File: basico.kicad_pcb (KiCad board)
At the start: 2 copper layers, 85.9 x 99.9 mm, 8 parts, among them P1 Power, P2 Analog, P3 Analog, P4 Digital, P5 PWM, P6 PWM, P7 Communication

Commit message: All routes done
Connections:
- P4 pad 1: GND -> (no net)
- P4 pad 2: GND -> (no net)
- P4 pad 35: +5V -> (no net)
- P4 pad 36: +5V -> (no net)
- XA101 pad 1: +3.3VP -> (no net)
- XA101 pad 2: +5V -> (no net)
- XA101 pad 20: GND -> (no net)
- XA101 pad 22: GND -> (no net)
- XA101 pad 24: GND -> (no net)
- XA101 pad 26: GND -> (no net)
- XA101 pad 28: GND -> (no net)
- XA101 pad 30: GND -> (no net)
- XA101 pad 32: GND -> (no net)
- XA101 pad 38: GND -> (no net)
- XA101 pad 4: GND -> (no net)
- XA101 pad 40: GND -> (no net)
- XA101 pad 51: GND -> (no net)
- XA101 pad 53: GND -> (no net)
- XA101 pad 57: GND -> (no net)
- XA101 pad 59: GND -> (no net)
- XA101 pad 65: GND -> (no net)
- XA101 pad 67: GND -> (no net)
- XA101 pad 77: GND -> (no net)
- XA101 pad 79: GND -> (no net)
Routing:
- net /Ar_38: track 0.00 -> 154.9 mm, vias 0 -> 2
- net /Ar_34: track 0.00 -> 120.1 mm, vias 0 -> 1
- net /Ar_17: track 0.00 -> 109.1 mm, vias 0 -> 1
- net /Ar_42: track 0.00 -> 88.5 mm, vias 0 -> 1
- net /Ar_A4: track 0.00 -> 77.7 mm, vias 0 -> 1
- net /Ar_11: track 0.00 -> 75.5 mm
- net /Ar_36: track 0.00 -> 73.3 mm
- net /Ar_16: track 0.00 -> 69.6 mm
- net /Ar_4: track 0.00 -> 69.3 mm
- net /Ar_A11: track 0.00 -> 67.9 mm, vias 0 -> 1
- net /Ar_A10: track 0.00 -> 66.2 mm, vias 0 -> 1
- net /Ar_A9: track 0.00 -> 64.8 mm
- net /Ar_10: track 0.00 -> 61.8 mm, vias 0 -> 1
- net /Ar_51: track 0.00 -> 56.8 mm
- net /Ar_9: track 0.00 -> 54.3 mm
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- added copper zone on B.Cu, net GND

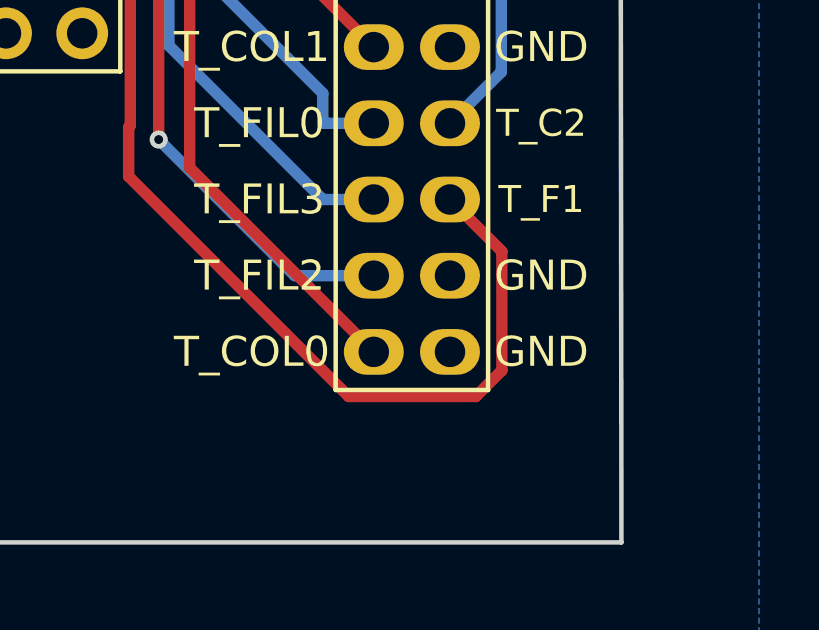
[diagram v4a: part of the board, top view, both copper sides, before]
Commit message: Fix unconnected pin
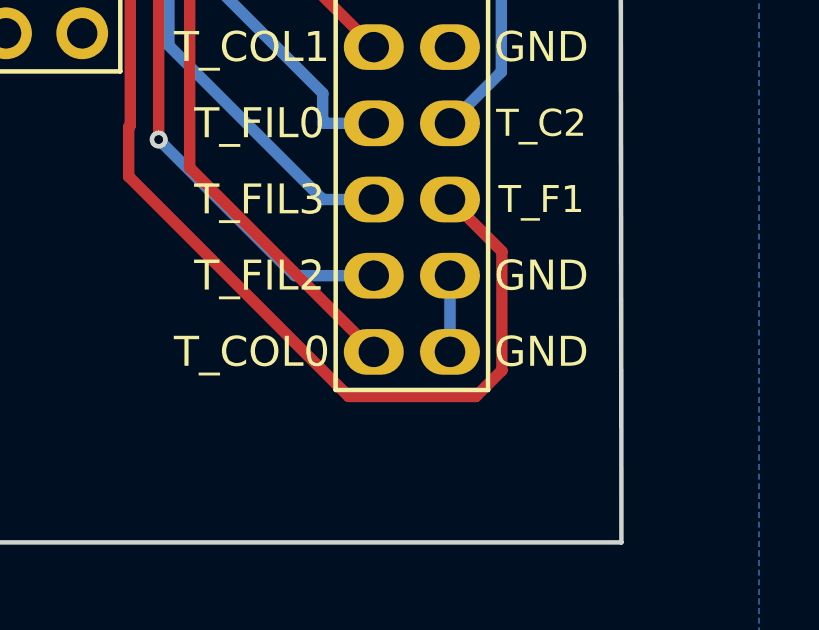
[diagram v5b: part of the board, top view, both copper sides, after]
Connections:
- XA101 pad 38: (no net) -> GND
- XA101 pad 40: (no net) -> GND
- XA101 pad 43: GND -> (no net)
- XA101 pad 45: GND -> (no net)
- XA101 pad 47: GND -> (no net)
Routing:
- net GND: track 0.00 -> 2.62 mm
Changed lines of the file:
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@@
     (thickness 1.6)
     (drawings 35)
-    (tracks 302)
+    (tracks 304)
     (zones 0)
     (modules 8)
@@
     (pad 36 thru_hole oval (at 2.54 43.18 270) (size 1.524 2) (drill 1.016) (layers *.Cu *.Mask F.SilkS)
       (net 16 /Ar_26))
-    (pad 38 thru_hole oval (at 2.54 45.72 270) (size 1.524 2) (drill 1.016) (layers *.Cu *.Mask F.SilkS))
+    (pad 38 thru_hole oval (at 2.54 45.72 270) (size 1.524 2) (drill 1.016) (layers *.Cu *.Mask F.SilkS)
+      (net 2 GND))
     (pad 35 thru_hole oval (at 0 43.18 270) (size 1.524 2) (drill 1.016) (layers *.Cu *.Mask F.SilkS)
       (net 15 /Ar_24))
@@
     (pad 39 thru_hole oval (at 0 48.26 270) (size 1.524 2) (drill 1.016) (layers *.Cu *.Mask F.SilkS)
       (net 43 /Ar_14))
-    (pad 40 thru_hole oval (at 2.54 48.26 270) (size 1.524 2) (drill 1.016) (layers *.Cu *.Mask F.SilkS))
+    (pad 40 thru_hole oval (at 2.54 48.26 270) (size 1.524 2) (drill 1.016) (layers *.Cu *.Mask F.SilkS)
+      (net 2 GND))
     (pad 30 thru_hole oval (at 2.54 35.56 270) (size 1.524 2) (drill 1.016) (layers *.Cu *.Mask F.SilkS))
     (pad 41 thru_hole rect (at -71.12 0 270) (size 1.524 2) (drill 1.016) (layers *.Cu *.Mask F.SilkS)
@@
     (pad 42 thru_hole oval (at -68.58 0 270) (size 1.524 2) (drill 1.016) (layers *.Cu *.Mask F.SilkS)
       (net 1 +5V))
-    (pad 43 thru_hole oval (at -71.12 2.54 270) (size 1.524 2) (drill 1.016) (layers *.Cu *.Mask F.SilkS)
-      (net 2 GND))
+    (pad 43 thru_hole oval (at -71.12 2.54 270) (size 1.524 2) (drill 1.016) (layers *.Cu *.Mask F.SilkS))
     (pad 44 thru_hole oval (at -68.58 2.54 270) (size 1.524 2) (drill 1.016) (layers *.Cu *.Mask F.SilkS)
       (net 12 /Ar_A0))
-    (pad 45 thru_hole oval (at -71.12 5.08 270) (size 1.524 2) (drill 1.016) (layers *.Cu *.Mask F.SilkS)
-      (net 2 GND))
+    (pad 45 thru_hole oval (at -71.12 5.08 270) (size 1.524 2) (drill 1.016) (layers *.Cu *.Mask F.SilkS))
     (pad 46 thru_hole oval (at -68.58 5.08 270) (size 1.524 2) (drill 1.016) (layers *.Cu *.Mask F.SilkS)
       (net 11 /Ar_A1))
-    (pad 47 thru_hole oval (at -71.12 7.62 270) (size 1.524 2) (drill 1.016) (layers *.Cu *.Mask F.SilkS)
-      (net 2 GND))
+    (pad 47 thru_hole oval (at -71.12 7.62 270) (size 1.524 2) (drill 1.016) (layers *.Cu *.Mask F.SilkS))
     (pad 48 thru_hole oval (at -68.58 7.62 270) (size 1.524 2) (drill 1.016) (layers *.Cu *.Mask F.SilkS)
       (net 10 /Ar_A2))
@@
   (segment (start 68.58 86.36) (end 68.58 76.16) (width 0.381) (layer F.Cu) (net 1))
   (segment (start 68.58 76.16) (end 79.16 65.58) (width 0.381) (layer F.Cu) (net 1))
+  (segment (start 139.7 132.08) (end 139.7 134.62) (width 0.381) (layer B.Cu) (net 2))
+  (segment (start 139.7 134.62) (end 139.7 134.7) (width 0.381) (layer B.Cu) (net 2))
   (segment (start 66.04 86.36) (end 66.04 76.16) (width 0.381) (layer F.Cu) (net 3))
   (segment (start 66.04 76.16) (end 79.16 63.04) (width 0.381) (layer F.Cu) (net 3))

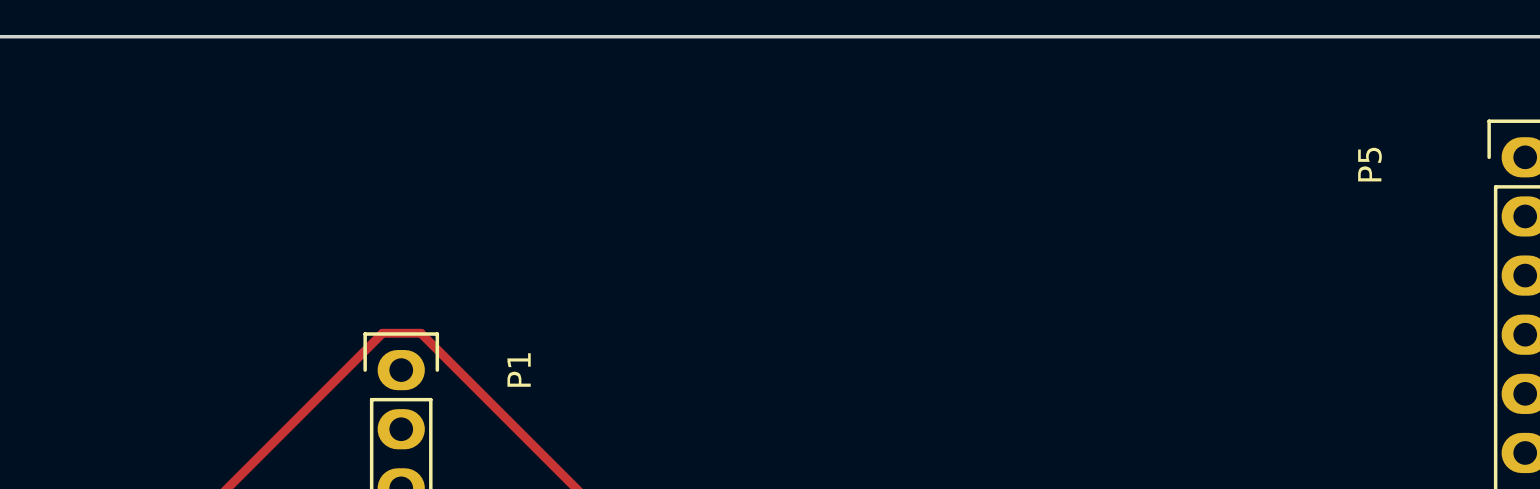
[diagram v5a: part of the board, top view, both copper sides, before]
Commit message: Clean up and add copper text
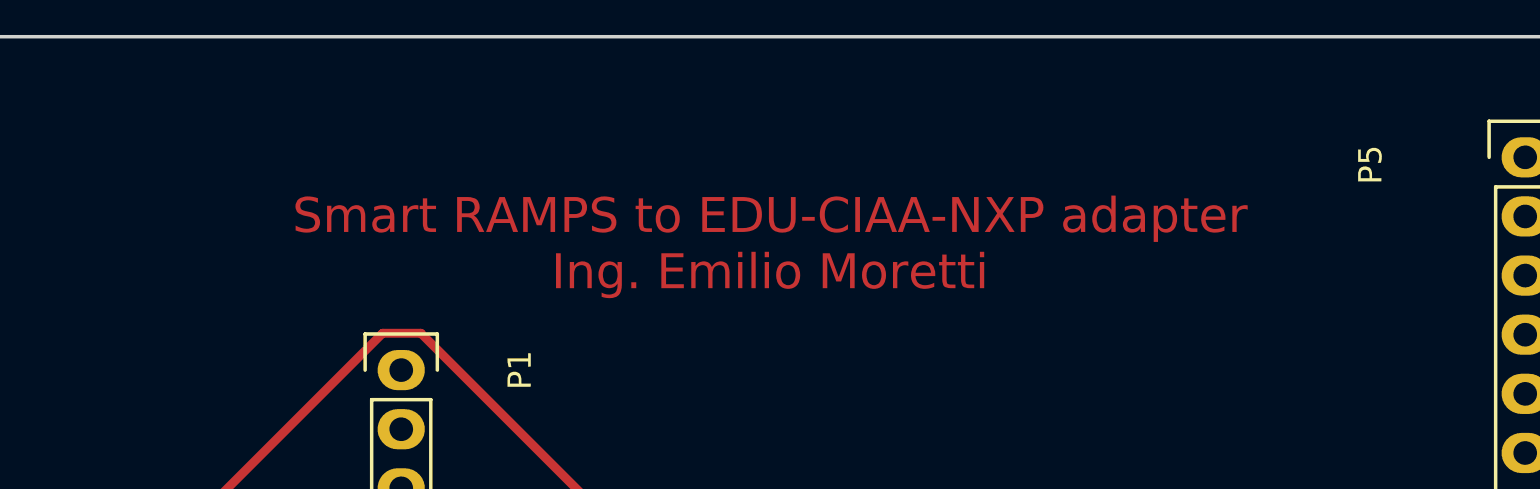
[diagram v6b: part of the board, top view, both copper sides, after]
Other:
- board text added: "Smart RAMPS to EDU-CIAA-NXP adapter Ing. Emilio Moretti"
- board text removed: "Borrar (Footprint MP1) la Plantilla-EDU-CIAA al finalizar el posicionamiento y definido el borde de PCB."
- board text removed: "Editar el rótulo"
- board text removed: "Editar este cuadro para reflejar cantidad de capas, si se han realizado cálculos de impedancia o si es relevante para el funcionamiento."
- board text removed: "Se sugiere colocar Nombre de Poncho y autor en cobre, serigrafía y rótulo."
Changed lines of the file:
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@@
   (general
     (thickness 1.6)
-    (drawings 35)
+    (drawings 20)
     (tracks 304)
     (zones 0)
@@
     )
   )
+  (gr_text "Smart RAMPS to EDU-CIAA-NXP adapter\nIng. Emilio Moretti" (at 95 50) (layer F.Cu)
+    (effects (font (size 1.5 1.5) (thickness 0.3)))
+  )
   (gr_line (start 59.69 140.97) (end 59.5 41.1) (angle 90) (layer Edge.Cuts) (width 0.15))
   (gr_line (start 81.28 140.97) (end 59.69 140.97) (angle 90) (layer Edge.Cuts) (width 0.15))
@@
   (gr_line (start 145.3 41.1) (end 145.415 140.97) (angle 90) (layer Edge.Cuts) (width 0.15))
   (gr_line (start 59.5 41.1) (end 145.3 41.1) (angle 90) (layer Edge.Cuts) (width 0.15))
-  (gr_line (start 228.6 163.83) (end 227.965 163.195) (angle 90) (layer Dwgs.User) (width 0.2))
-  (gr_line (start 229.235 163.195) (end 228.6 163.83) (angle 90) (layer Dwgs.User) (width 0.2))
-  (gr_line (start 228.6 163.83) (end 229.235 163.195) (angle 90) (layer Dwgs.User) (width 0.2))
-  (gr_line (start 228.6 153.035) (end 228.6 163.83) (angle 90) (layer Dwgs.User) (width 0.2))
-  (gr_line (start 223.52 153.035) (end 228.6 153.035) (angle 90) (layer Dwgs.User) (width 0.2))
-  (gr_text "Editar el rótulo" (at 213.36 153.035) (layer Dwgs.User)
-    (effects (font (size 1.5 1.5) (thickness 0.3)))
-  )
-  (gr_line (start 172.085 96.52) (end 172.72 97.155) (angle 90) (layer Dwgs.User) (width 0.2))
-  (gr_line (start 172.085 96.52) (end 172.72 95.885) (angle 90) (layer Dwgs.User) (width 0.2))
-  (gr_line (start 201.295 96.52) (end 172.085 96.52) (angle 90) (layer Dwgs.User) (width 0.2))
-  (gr_text "Se sugiere colocar Nombre  de \nPoncho  y autor en cobre, \nserigrafía y rótulo." (at 201.93 96.52) (layer Dwgs.User)
-    (effects (font (size 1.5 1.5) (thickness 0.3)) (justify left))
-  )
-  (gr_text "Editar este cuadro para reflejar \ncantidad de capas, si se han \nrealizado cálculos de impedancia o\nsi es relevante para el funcionamiento." (at 253.365 45.085) (layer Dwgs.User)
-    (effects (font (size 1.5 1.5) (thickness 0.3)))
-  )
   (gr_text "Diseño simple faz.\nSin requerimientos especiales." (at 194.945 24.13) (layer Dwgs.User)
     (effects (font (size 1.5 1.5) (thickness 0.3)) (justify left))
@@
   (gr_line (start 186.055 53.975) (end 279.4 53.975) (angle 90) (layer Dwgs.User) (width 0.2))
   (gr_line (start 186.055 15.875) (end 186.055 53.975) (angle 90) (layer Dwgs.User) (width 0.2))
-  (gr_line (start 151.765 59.69) (end 153.035 60.96) (angle 90) (layer Dwgs.User) (width 0.2))
-  (gr_line (start 153.035 58.42) (end 151.765 59.69) (angle 90) (layer Dwgs.User) (width 0.2))
-  (gr_line (start 151.765 59.69) (end 153.035 58.42) (angle 90) (layer Dwgs.User) (width 0.2))
-  (gr_line (start 200.66 59.69) (end 151.765 59.69) (angle 90) (layer Dwgs.User) (width 0.2))
-  (gr_text "Borrar (Footprint MP1) la Plantilla-EDU-CIAA \nal finalizar  el posicionamiento y definido el \nborde de PCB." (at 201.93 61.595) (layer Dwgs.User)
-    (effects (font (size 1.5 1.5) (thickness 0.3)) (justify left))
-  )
   (gr_text "PONCHO BASICO\nhttp://www.proyecto-ciaa.com.ar/" (at 37.465 20.32) (layer Dwgs.User)
     (effects (font (size 1.5 1.5) (thickness 0.3)))

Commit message: Update version number
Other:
- board text added: "Smart RAMPS to EDU-CIAA-NXP adapter v1.0 Ing. Emilio Moretti - 2019"
- board text removed: "Smart RAMPS to EDU-CIAA-NXP adapter Ing. Emilio Moretti"
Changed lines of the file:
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@@
     (add_net +3.3VP)
     (add_net +5V)
+    (add_net /Ar_0)
+    (add_net /Ar_1)
     (add_net /Ar_10)
     (add_net /Ar_11)
+    (add_net /Ar_12)
+    (add_net /Ar_13)
     (add_net /Ar_14)
+    (add_net /Ar_15)
     (add_net /Ar_16)
     (add_net /Ar_17)
     (add_net /Ar_18)
+    (add_net /Ar_19)
+    (add_net /Ar_2)
     (add_net /Ar_20)
     (add_net /Ar_21)
+    (add_net /Ar_22)
+    (add_net /Ar_23)
     (add_net /Ar_24)
+    (add_net /Ar_25)
     (add_net /Ar_26)
+    (add_net /Ar_27)
     (add_net /Ar_28)
+    (add_net /Ar_29)
     (add_net /Ar_3)
     (add_net /Ar_30)
+    (add_net /Ar_31)
+    (add_net /Ar_32)
+    (add_net /Ar_33)
     (add_net /Ar_34)
+    (add_net /Ar_35)
     (add_net /Ar_36)
+    (add_net /Ar_37)
     (add_net /Ar_38)
+    (add_net /Ar_39)
     (add_net /Ar_4)
     (add_net /Ar_40)
+    (add_net /Ar_41)
     (add_net /Ar_42)
+    (add_net /Ar_43)
     (add_net /Ar_44)
+    (add_net /Ar_45)
     (add_net /Ar_46)
+    (add_net /Ar_47)
     (add_net /Ar_48)
     (add_net /Ar_49)
+    (add_net /Ar_5)
     (add_net /Ar_50)
     (add_net /Ar_51)
     (add_net /Ar_52)
     (add_net /Ar_53)
+    (add_net /Ar_6)
+    (add_net /Ar_7)
     (add_net /Ar_8)
     (add_net /Ar_9)
@@
     (add_net /Ar_A10)
     (add_net /Ar_A11)
+    (add_net /Ar_A12)
     (add_net /Ar_A13)
+    (add_net /Ar_A14)
+    (add_net /Ar_A15)
     (add_net /Ar_A2)
     (add_net /Ar_A3)
@@
     (add_net /Ar_A8)
     (add_net /Ar_A9)
+    (add_net /Ar_AREF)
+    (add_net /Ar_IOREF)
+    (add_net /Ar_Reset)
+    (add_net /Ar_SCL)
+    (add_net /Ar_SDA)
+    (add_net /Ar_Vin)
     (add_net GND)
     (add_net GNDA)
+    (add_net "Net-(P1-Pad1)")
+    (add_net "Net-(P4-Pad1)")
+    (add_net "Net-(P4-Pad2)")
+    (add_net "Net-(P4-Pad35)")
+    (add_net "Net-(P4-Pad36)")
+    (add_net "Net-(XA101-Pad1)")
+    (add_net "Net-(XA101-Pad15)")
+    (add_net "Net-(XA101-Pad17)")
+    (add_net "Net-(XA101-Pad2)")
+    (add_net "Net-(XA101-Pad20)")
+    (add_net "Net-(XA101-Pad22)")
+    (add_net "Net-(XA101-Pad24)")
+    (add_net "Net-(XA101-Pad26)")
+    (add_net "Net-(XA101-Pad28)")
+    (add_net "Net-(XA101-Pad3)")
+    (add_net "Net-(XA101-Pad30)")
+    (add_net "Net-(XA101-Pad32)")
+    (add_net "Net-(XA101-Pad4)")
+    (add_net "Net-(XA101-Pad43)")
+    (add_net "Net-(XA101-Pad45)")
+    (add_net "Net-(XA101-Pad47)")
+    (add_net "Net-(XA101-Pad5)")
+    (add_net "Net-(XA101-Pad51)")
+    (add_net "Net-(XA101-Pad53)")
+    (add_net "Net-(XA101-Pad55)")
+    (add_net "Net-(XA101-Pad57)")
+    (add_net "Net-(XA101-Pad59)")
+    (add_net "Net-(XA101-Pad6)")
+    (add_net "Net-(XA101-Pad65)")
+    (add_net "Net-(XA101-Pad67)")
+    (add_net "Net-(XA101-Pad77)")
+    (add_net "Net-(XA101-Pad79)")
   )
   (module footprint:Socket_Strip_Arduino_1x08 (layer F.Cu)
@@
     )
   )
-  (gr_text "Smart RAMPS to EDU-CIAA-NXP adapter\nIng. Emilio Moretti" (at 95 50) (layer F.Cu)
+  (gr_text "Smart RAMPS to EDU-CIAA-NXP adapter v1.0\nIng. Emilio Moretti - 2019" (at 95 50) (layer F.Cu)
     (effects (font (size 1.5 1.5) (thickness 0.3)))
   )

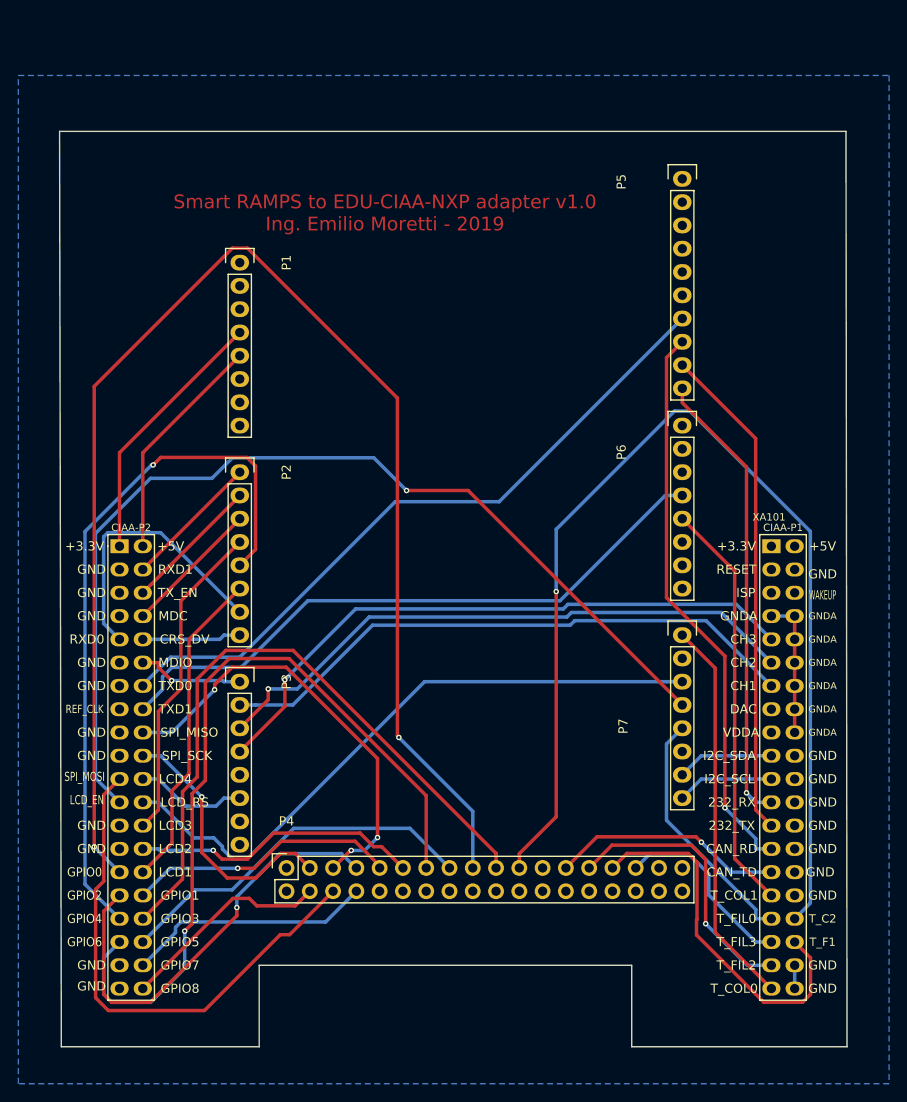
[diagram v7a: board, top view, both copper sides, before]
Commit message: Update arduino sizes
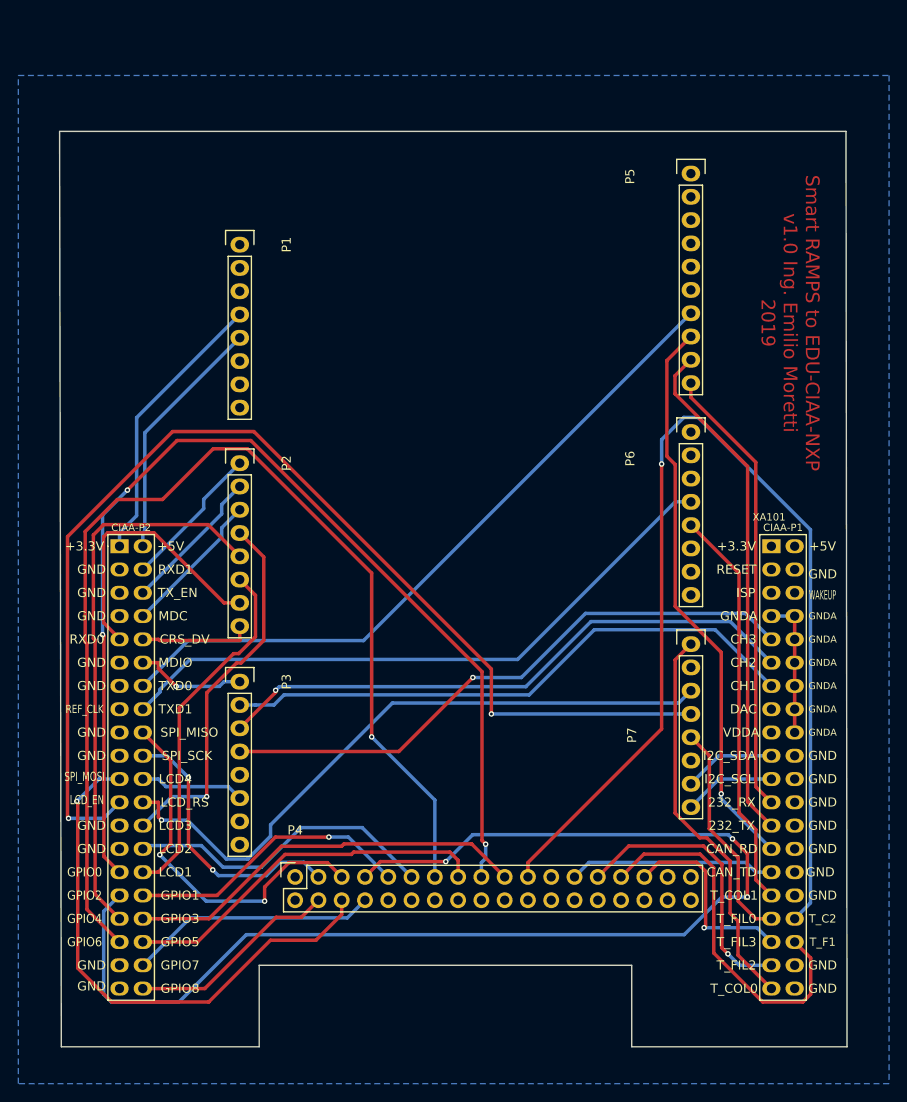
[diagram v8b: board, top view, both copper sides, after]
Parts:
- moved P1 1.96 mm to (79.2, 53.5)
- moved P7 1.36 mm to (128.4, 97.0)
- moved P4 1.36 mm to (85.2, 122.4)
- moved P6 1.18 mm to (128.4, 73.9)
- moved P5 1.10 mm to (128.4, 45.7)
- moved P2 0.98 mm to (79.2, 77.3)
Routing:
- net /Ar_48: track 48.0 -> 136.0 mm, vias 1 -> 3
- net /Ar_38: track 154.9 -> 117.7 mm, vias 2 -> 3
- net /Ar_42: track 88.5 -> 123.0 mm
- net /Ar_36: track 73.3 -> 44.4 mm
- net /Ar_A4: track 77.7 -> 60.9 mm, vias 1 -> 0
- net /Ar_17: track 109.1 -> 125.5 mm, vias 1 -> 2
- net /Ar_50: track 47.9 -> 40.3 mm, vias 3 -> 2
- net /Ar_A3: track 35.3 -> 41.0 mm, vias 0 -> 1
- net /Ar_A5: track 35.3 -> 39.0 mm
- net /Ar_51: track 56.8 -> 59.8 mm, vias 0 -> 1
- net /Ar_44: track 31.6 -> 34.5 mm, vias 1 -> 0
- net /Ar_30: track 25.4 -> 22.6 mm, vias 1 -> 0
- net /Ar_18: track 27.2 -> 24.4 mm
- net GND: track 2.62 -> 0.00 mm
- net /Ar_A11: track 67.9 -> 65.4 mm
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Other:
- board text added: "Smart RAMPS to EDU-CIAA-NXP v1.0 Ing. Emilio Moretti 2019"
- board text removed: "Smart RAMPS to EDU-CIAA-NXP adapter v1.0 Ing. Emilio Moretti - 2019"
